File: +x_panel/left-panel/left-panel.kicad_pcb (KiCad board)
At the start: 2 copper layers, 85 x 270 mm, 14 parts

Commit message: Rerouted some stuff
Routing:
- net Net-(Buck1-BCR+): track 65.2 -> 61.7 mm
- net Net-(Buck1-BCR-): track 292.1 -> 288.8 mm
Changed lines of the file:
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@@
-	)
-	(segment
-		(start 817.595 63.955)
-		(end 818.208274 63.955)
-		(width 3)
-		(layer "B.Cu")
-		(net 1)
-	)
-	(segment
-		(start 816.79 64.76)
-		(end 817.595 63.955)
-		(width 3)
-		(layer "B.Cu")
-		(net 1)
-	)
-	(segment
-		(start 816.79 65.48)
-		(end 816.79 64.76)
-		(width 3)
-		(layer "B.Cu")
-		(net 1)
 	)
 	(segment
 		(start 816.79 293.47)
-		(end 816.79 65.48)
+		(end 816.79 66.35)
 		(width 4)
 		(layer "B.Cu")
@@
 	)
 	(segment
-		(start 817.934 60.754)
-		(end 818.208274 60.754)
-		(width 3)
-		(layer "B.Cu")
-		(net 2)
-	)
-	(segment
 		(start 817.57 48.61)
-		(end 817.57 60.39)
-		(width 3)
-		(layer "B.Cu")
-		(net 2)
-	)
-	(segment
-		(start 817.57 60.39)
-		(end 817.934 60.754)
+		(end 817.57 57.7)
 		(width 3)
 		(layer "B.Cu")
@@
 	)
 	(zone
-		(net 2)
-		(net_name "Net-(Buck1-BCR+)")
+		(net 1)
+		(net_name "Net-(Buck1-BCR-)")
 		(layer "B.Cu")
 		(hatch edge 0.5)
-		(priority 1)
-		(connect_pads
+		(priority 17540)
+		(connect_pads yes
 			(clearance 0)
 		)
-		(min_thickness 0.25)
+		(min_thickness 0.0254)
 		(filled_areas_thickness no)
 		(fill yes
 			(thermal_gap 0.5)
 			(thermal_bridge_width 0.5)
-			(island_removal_mode 1)
-			(island_area_min 10)
 		)
 		(polygon
 			(pts
-				(xy 818.43 58.89) (xy 818.683685 61.86174) (xy 818.46 61.86) (xy 817.44 61.85) (xy 817.460757 61.86259)
-				(xy 816.713351 59.294888) (xy 818.95 59.05)
+				(xy 816.79 66.65) (xy 818.79 66.35705) (xy 818.789667 65.959805) (xy 818.790459 65.613771) (xy 818.795066 65.309381)
+				(xy 818.806173 65.037066) (xy 818.826469 64.787259) (xy 818.858641 64.550392) (xy 818.905377 64.316897)
+				(xy 818.969364 64.077207) (xy 819.053291 63.821754) (xy 819.225 63.175) (xy 819.225 62.9) (xy 818.25399 62.693312)
+				(xy 817.183274 62.8075) (xy 817.183274 63.16) (xy 817.116262 63.559521) (xy 816.934373 63.875879)
+				(xy 816.666326 64.133609) (xy 816.340841 64.357246) (xy 815.986637 64.571324) (xy 815.632432 64.800378)
+				(xy 815.306947 65.068943) (xy 815.0389 65.401554) (xy 814.857011 65.822744) (xy 814.79 66.35705)
 			)
 		)
 	)
 	(zone
-		(net 1)
-		(net_name "Net-(Buck1-BCR-)")
+		(net 2)
+		(net_name "Net-(Buck1-BCR+)")
 		(layer "B.Cu")
 		(hatch edge 0.5)
-		(connect_pads
+		(priority 17540)
+		(connect_pads yes
 			(clearance 0)
 		)
-		(min_thickness 0.25)
+		(min_thickness 0.0254)
 		(filled_areas_thickness no)
 		(fill yes
 			(thermal_gap 0.5)
 			(thermal_bridge_width 0.5)
-			(island_removal_mode 1)
-			(island_area_min 10)
 		)
 		(polygon
 			(pts
-				(xy 816.7 62.79) (xy 815.740318 65.518735) (xy 819.29 65.52) (xy 819.011399 62.678607)
+				(xy 817.57 57.475) (xy 816.07 57.69305) (xy 816.101171 58.201709) (xy 816.18578 58.633024) (xy 816.310467 59.002876)
+				(xy 816.461872 59.327147) (xy 816.626637 59.62172) (xy 816.791401 59.902478) (xy 816.942806 60.185302)
+				(xy 817.067493 60.486076) (xy 817.152102 60.820681) (xy 817.183274 61.205) (xy 817.183274 61.5525)
+				(xy 818.228378 61.673845) (xy 819.219489 61.384964) (xy 819.219489 61.037464) (xy 819.16544 60.688053)
+				(xy 819.125146 60.374743) (xy 819.096707 60.085244) (xy 819.078224 59.807264) (xy 819.067795 59.528514)
+				(xy 819.063523 59.236703) (xy 819.063507 58.919542) (xy 819.065848 58.564739) (xy 819.068645 58.160005)
+				(xy 819.07 57.69305)
 			)
 		)

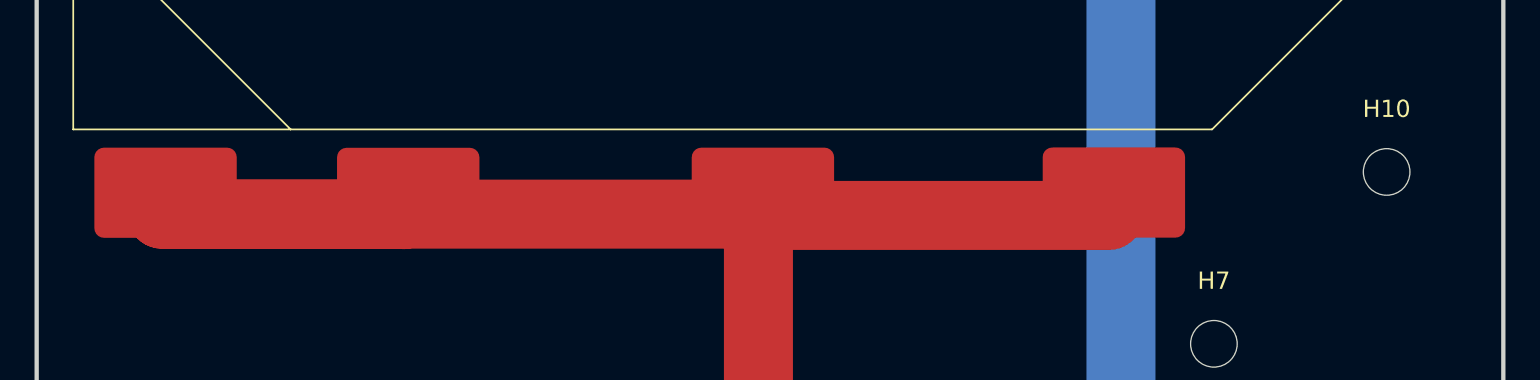
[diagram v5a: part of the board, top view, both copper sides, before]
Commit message: removed solder mask from footprint
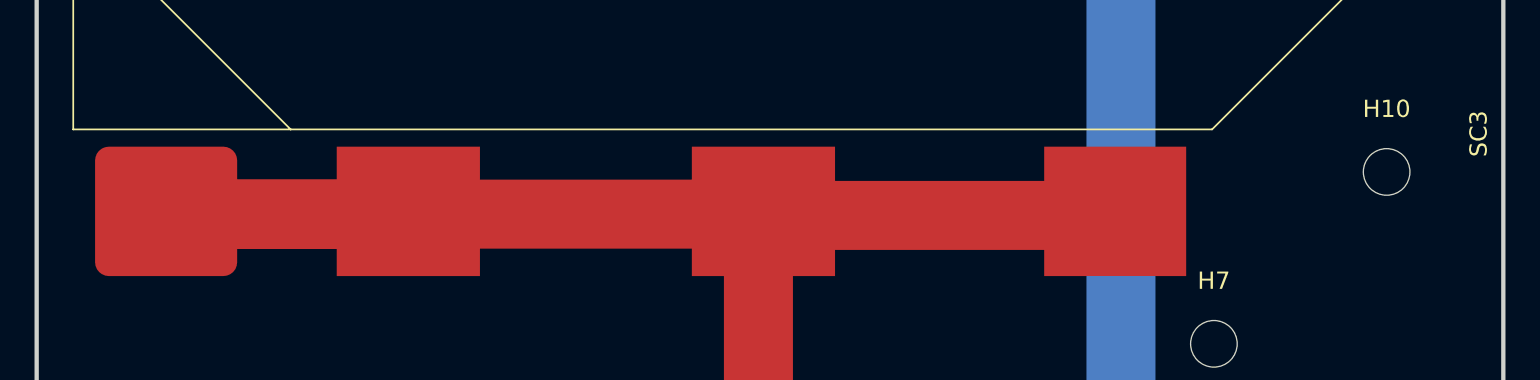
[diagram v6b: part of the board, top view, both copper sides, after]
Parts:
- SC3: footprint Solar_cell:Solar_Cell_Lightricity_S8040_CIC_Shorter_Tabs -> Solar_cell:Solar_Cell_Lightricity_S8040_CIC

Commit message: reviewed boards
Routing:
- net Net-(Buck1-BCR-): track 288.8 -> 296.0 mm
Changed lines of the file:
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@@
 	)
 	(segment
-		(start 816.82 300.115)
-		(end 816.82 293.5)
+		(start 806.19 300.115)
+		(end 796.435 300.115)
 		(width 4)
 		(layer "F.Cu")
@@
 	)
 	(segment
-		(start 816.82 293.5)
-		(end 816.79 293.47)
+		(start 806.215 300.09)
+		(end 816.795 300.09)
 		(width 4)
 		(layer "F.Cu")
@@
 	)
 	(segment
-		(start 816.82 300.115)
-		(end 796.435 300.115)
+		(start 816.795 300.09)
+		(end 816.82 300.115)
 		(width 4)
 		(layer "F.Cu")
@@
 	)
 	(via
-		(at 816.79 293.47)
+		(at 806.215 300.09)
 		(size 4)
 		(drill 2)
@@
 	)
 	(segment
-		(start 816.79 293.47)
+		(start 816.79 294.49)
 		(end 816.79 66.35)
 		(width 4)
 		(layer "B.Cu")
+		(net 1)
+	)
+	(segment
+		(start 806.215 300.09)
+		(end 811.19 300.09)
+		(width 4)
+		(layer "B.Cu")
+		(net 1)
+	)
+	(segment
+		(start 811.19 300.09)
+		(end 816.79 294.49)
+		(width 4)
+		(layer "B.Cu")
